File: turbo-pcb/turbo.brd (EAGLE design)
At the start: 54 x 51.4 mm, 4 parts

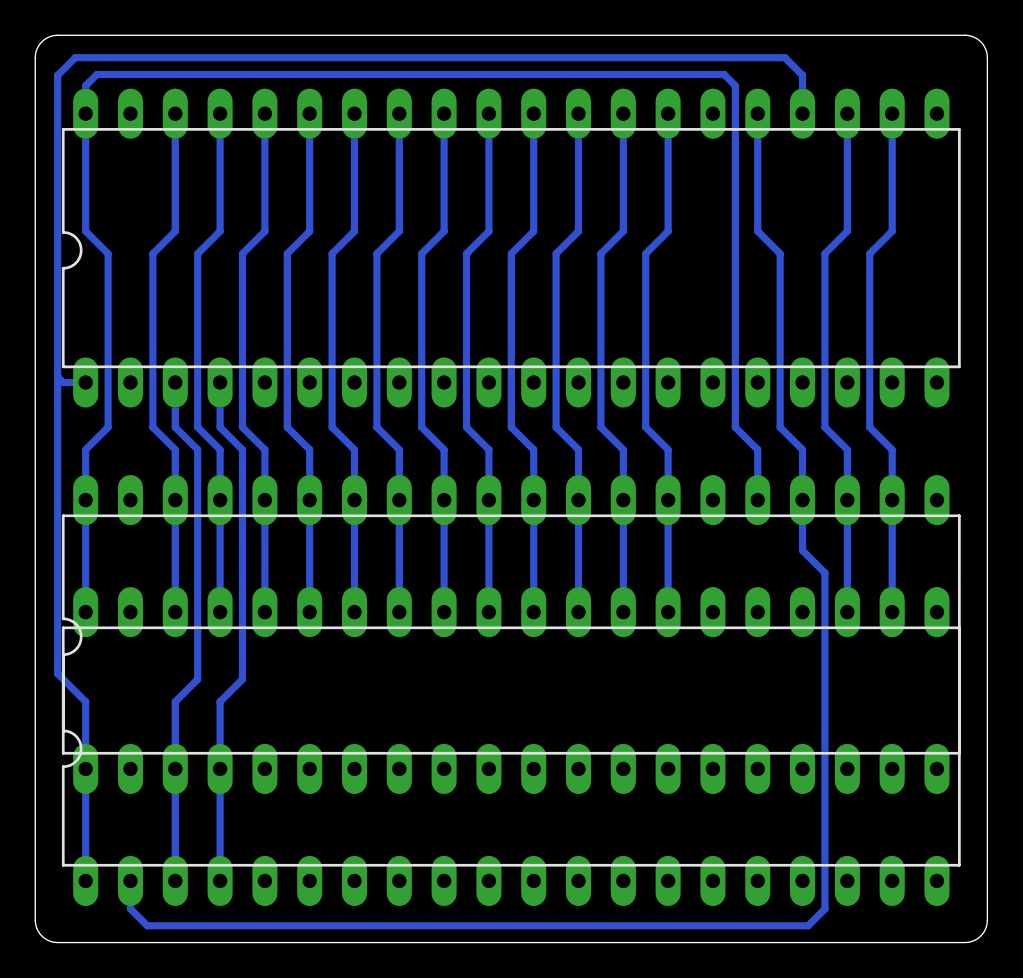
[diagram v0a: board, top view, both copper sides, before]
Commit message: shrink the board a little
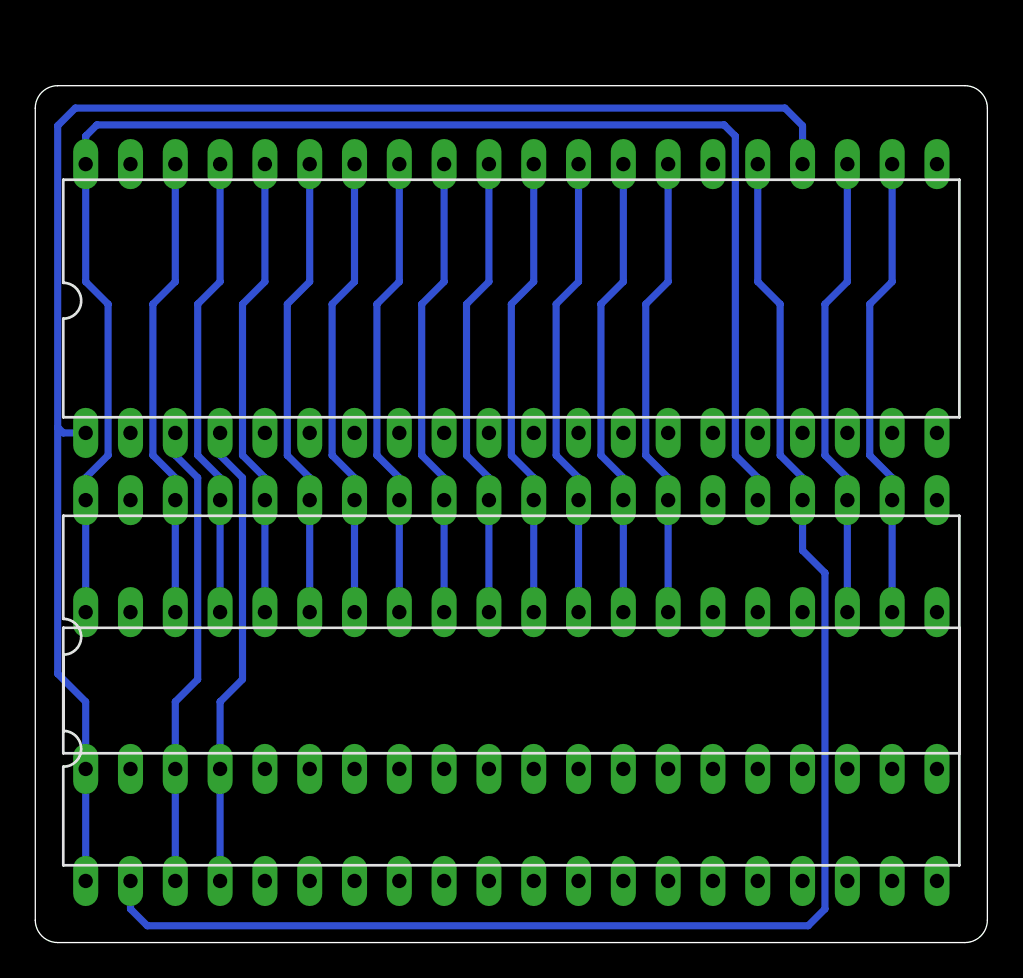
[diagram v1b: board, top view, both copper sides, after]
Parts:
- moved AY2 2.86 mm to (116.5, 28.9)
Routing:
- net VCC: track 92.3 -> 86.6 mm
- net GND: track 93.3 -> 90.4 mm
- net A4: track 88.4 -> 85.6 mm
- net B: track 29.3 -> 26.5 mm
- net A: track 29.3 -> 26.5 mm
- net D7: track 29.3 -> 26.5 mm
- net D6: track 29.3 -> 26.5 mm
- net D5: track 29.3 -> 26.5 mm
- net D4: track 29.3 -> 26.5 mm
- net D3: track 29.3 -> 26.5 mm
- net D2: track 29.3 -> 26.5 mm
- net D1: track 29.3 -> 26.5 mm
- net D0: track 29.3 -> 26.5 mm
- net CLK: track 29.3 -> 26.5 mm
- net C: track 29.3 -> 26.5 mm
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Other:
- board size 54 x 51.4 mm -> 54 x 48.6 mm
